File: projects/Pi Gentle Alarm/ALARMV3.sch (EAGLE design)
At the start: 6 parts, among them IC1 7805T, X1 RASPI_BOARD_B+_E0

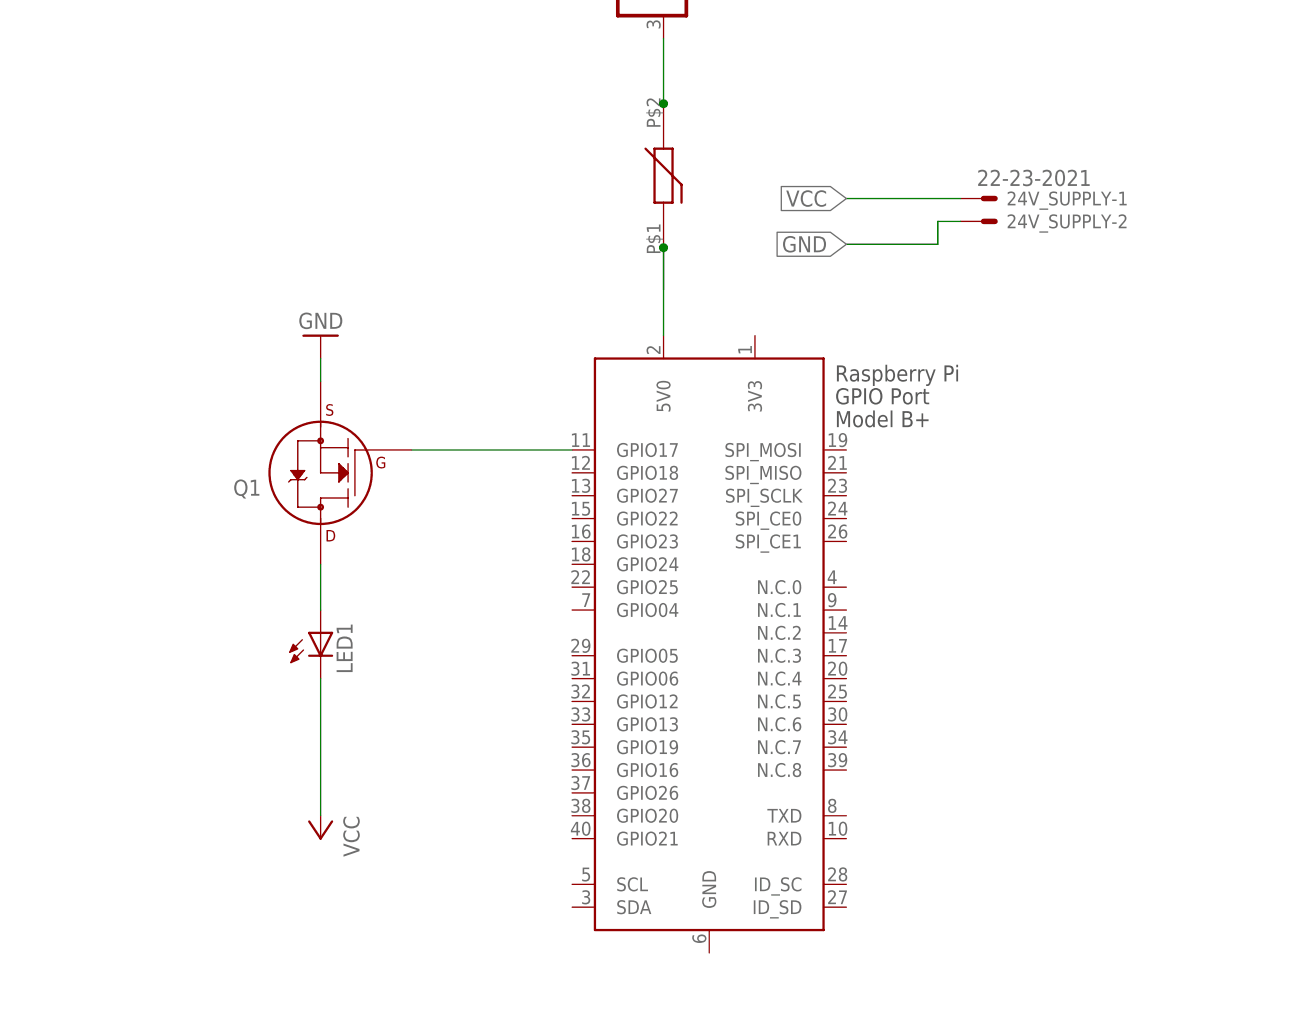
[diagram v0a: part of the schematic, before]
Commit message: Added a button for turning off the alarm
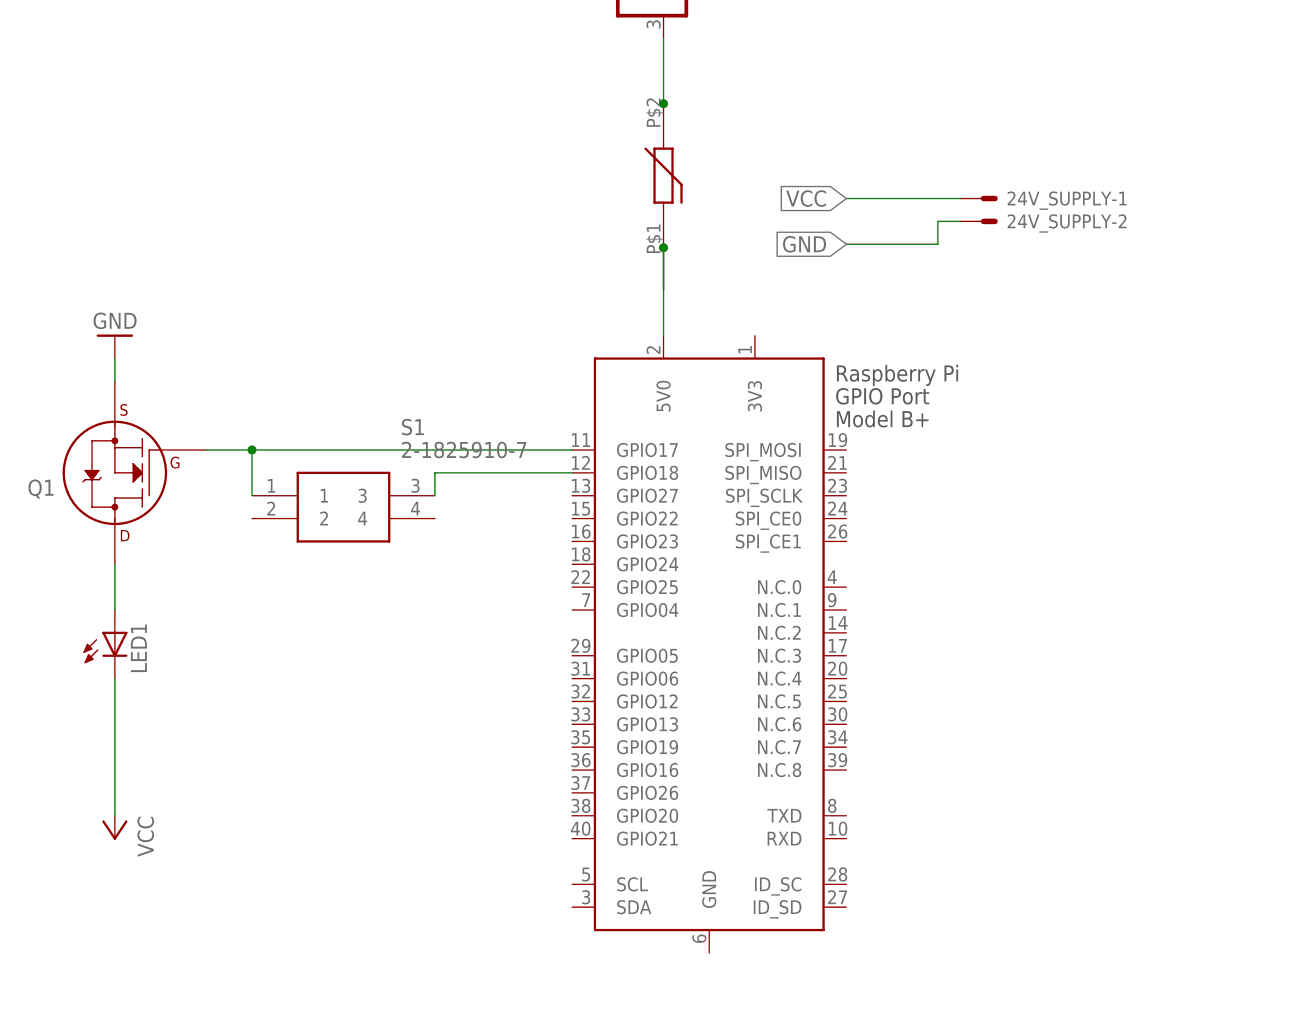
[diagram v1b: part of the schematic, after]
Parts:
- added S1: 2-1825910-7, SamacSys_Parts:2-1825910-7
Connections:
- new net N$3: S1.3, X1.GPIO18
- net GPIO17: now also S1.1
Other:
- moved on the sheet: LED1, Q1
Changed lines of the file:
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@@
 <part name="GND2" library="supply1" library_urn="urn:adsk.eagle:library:371" deviceset="GND" device=""/>
 <part name="F1" library="Test" deviceset="MF-MSMF260-2" device=""/>
+<part name="S1" library="SamacSys_Parts" deviceset="2-1825910-7" device=""/>
 </parts>
 <sheets>
@@
 <instance part="24V_SUPPLY" gate="-1" x="119.38" y="198.12" smashed="yes">
 <attribute name="NAME" x="121.92" y="197.358" size="1.524" layer="95"/>
-<attribute name="VALUE" x="118.618" y="199.517" size="1.778" layer="96"/>
 </instance>
 <instance part="24V_SUPPLY" gate="-2" x="119.38" y="195.58" smashed="yes">
 <attribute name="NAME" x="121.92" y="194.818" size="1.524" layer="95"/>
 </instance>
-<instance part="Q1" gate="G$1" x="45.72" y="167.64" smashed="yes" rot="R180">
-<attribute name="NAME" x="39.116" y="166.878" size="1.778" layer="95" rot="R180"/>
-<attribute name="VALUE" x="39.116" y="169.164" size="1.778" layer="96" rot="R180"/>
-<attribute name="OC_NEWARK" x="45.72" y="167.64" size="1.778" layer="96" display="off"/>
-<attribute name="MF" x="45.72" y="167.64" size="1.778" layer="96" display="off"/>
-<attribute name="MPN" x="45.72" y="167.64" size="1.778" layer="96" display="off"/>
+<instance part="Q1" gate="G$1" x="22.86" y="167.64" smashed="yes" rot="R180">
+<attribute name="NAME" x="16.256" y="166.878" size="1.778" layer="95" rot="R180"/>
+<attribute name="VALUE" x="16.256" y="169.164" size="1.778" layer="96" rot="R180"/>
+<attribute name="OC_NEWARK" x="22.86" y="167.64" size="1.778" layer="96" display="off"/>
+<attribute name="MF" x="22.86" y="167.64" size="1.778" layer="96" display="off"/>
+<attribute name="MPN" x="22.86" y="167.64" size="1.778" layer="96" display="off"/>
 </instance>
-<instance part="P+1" gate="VCC" x="45.72" y="127" smashed="yes" rot="R180">
-<attribute name="VALUE" x="48.26" y="129.54" size="1.778" layer="96" rot="R270"/>
+<instance part="P+1" gate="VCC" x="22.86" y="127" smashed="yes" rot="R180">
+<attribute name="VALUE" x="25.4" y="129.54" size="1.778" layer="96" rot="R270"/>
 </instance>
-<instance part="GND1" gate="1" x="45.72" y="182.88" smashed="yes" rot="R180">
-<attribute name="VALUE" x="48.26" y="185.42" size="1.778" layer="96" rot="R180"/>
+<instance part="GND1" gate="1" x="22.86" y="182.88" smashed="yes" rot="R180">
+<attribute name="VALUE" x="25.4" y="185.42" size="1.778" layer="96" rot="R180"/>
 </instance>
-<instance part="LED1" gate="G$1" x="45.72" y="149.86" smashed="yes">
-<attribute name="NAME" x="49.276" y="145.288" size="1.778" layer="95" rot="R90"/>
-<attribute name="VALUE" x="51.435" y="145.288" size="1.778" layer="96" rot="R90"/>
-<attribute name="OC_NEWARK" x="45.72" y="149.86" size="1.778" layer="96" display="off"/>
-<attribute name="MF" x="45.72" y="149.86" size="1.778" layer="96" display="off"/>
-<attribute name="MPN" x="45.72" y="149.86" size="1.778" layer="96" display="off"/>
+<instance part="LED1" gate="G$1" x="22.86" y="149.86" smashed="yes">
+<attribute name="NAME" x="26.416" y="145.288" size="1.778" layer="95" rot="R90"/>
+<attribute name="VALUE" x="28.575" y="145.288" size="1.778" layer="96" rot="R90"/>
+<attribute name="OC_NEWARK" x="22.86" y="149.86" size="1.778" layer="96" display="off"/>
+<attribute name="MF" x="22.86" y="149.86" size="1.778" layer="96" display="off"/>
+<attribute name="MPN" x="22.86" y="149.86" size="1.778" layer="96" display="off"/>
 </instance>
 <instance part="IC1" gate="A1" x="83.82" y="226.06" smashed="yes" rot="R270">
@@
 </instance>
 <instance part="F1" gate="G$1" x="83.82" y="200.66" smashed="yes" rot="R90"/>
+<instance part="S1" gate="G$1" x="38.1" y="165.1" smashed="yes">
+<attribute name="NAME" x="54.61" y="172.72" size="1.778" layer="95" align="center-left"/>
+<attribute name="VALUE" x="54.61" y="170.18" size="1.778" layer="96" align="center-left"/>
+</instance>
 </instances>
 <busses>
@@
 <segment>
 <pinref part="P+1" gate="VCC" pin="VCC"/>
-<wire x1="45.72" y1="144.78" x2="45.72" y2="129.54" width="0.1524" layer="91"/>
+<wire x1="22.86" y1="144.78" x2="22.86" y2="129.54" width="0.1524" layer="91"/>
 <pinref part="LED1" gate="G$1" pin="C"/>
 </segment>
@@
 <pinref part="Q1" gate="G$1" pin="S"/>
 <pinref part="GND1" gate="1" pin="GND"/>
-<wire x1="45.72" y1="177.8" x2="45.72" y2="180.34" width="0.1524" layer="91"/>
+<wire x1="22.86" y1="177.8" x2="22.86" y2="180.34" width="0.1524" layer="91"/>
 </segment>
 <segment>
@@
 <net name="GPIO17" class="0">
 <segment>
-<wire x1="73.66" y1="170.18" x2="55.88" y2="170.18" width="0.1524" layer="91"/>
+<wire x1="73.66" y1="170.18" x2="38.1" y2="170.18" width="0.1524" layer="91"/>
 <pinref part="Q1" gate="G$1" pin="G"/>
 <pinref part="X1" gate="G$1" pin="GPIO17"/>
+<pinref part="S1" gate="G$1" pin="1"/>
+<wire x1="38.1" y1="170.18" x2="33.02" y2="170.18" width="0.1524" layer="91"/>
+<wire x1="38.1" y1="165.1" x2="38.1" y2="170.18" width="0.1524" layer="91"/>
+<junction x="38.1" y="170.18"/>
 </segment>
 </net>
@@
 <segment>
 <pinref part="Q1" gate="G$1" pin="D"/>
-<wire x1="45.72" y1="152.4" x2="45.72" y2="157.48" width="0.1524" layer="91"/>
+<wire x1="22.86" y1="152.4" x2="22.86" y2="157.48" width="0.1524" layer="91"/>
 <pinref part="LED1" gate="G$1" pin="A"/>
 </segment>
@@
 </segment>
 </net>
+<net name="N$3" class="0">
+<segment>
+<pinref part="S1" gate="G$1" pin="3"/>
+<pinref part="X1" gate="G$1" pin="GPIO18"/>
+<wire x1="58.42" y1="165.1" x2="58.42" y2="167.64" width="0.1524" layer="91"/>
+<wire x1="58.42" y1="167.64" x2="73.66" y2="167.64" width="0.1524" layer="91"/>
+</segment>
+</net>

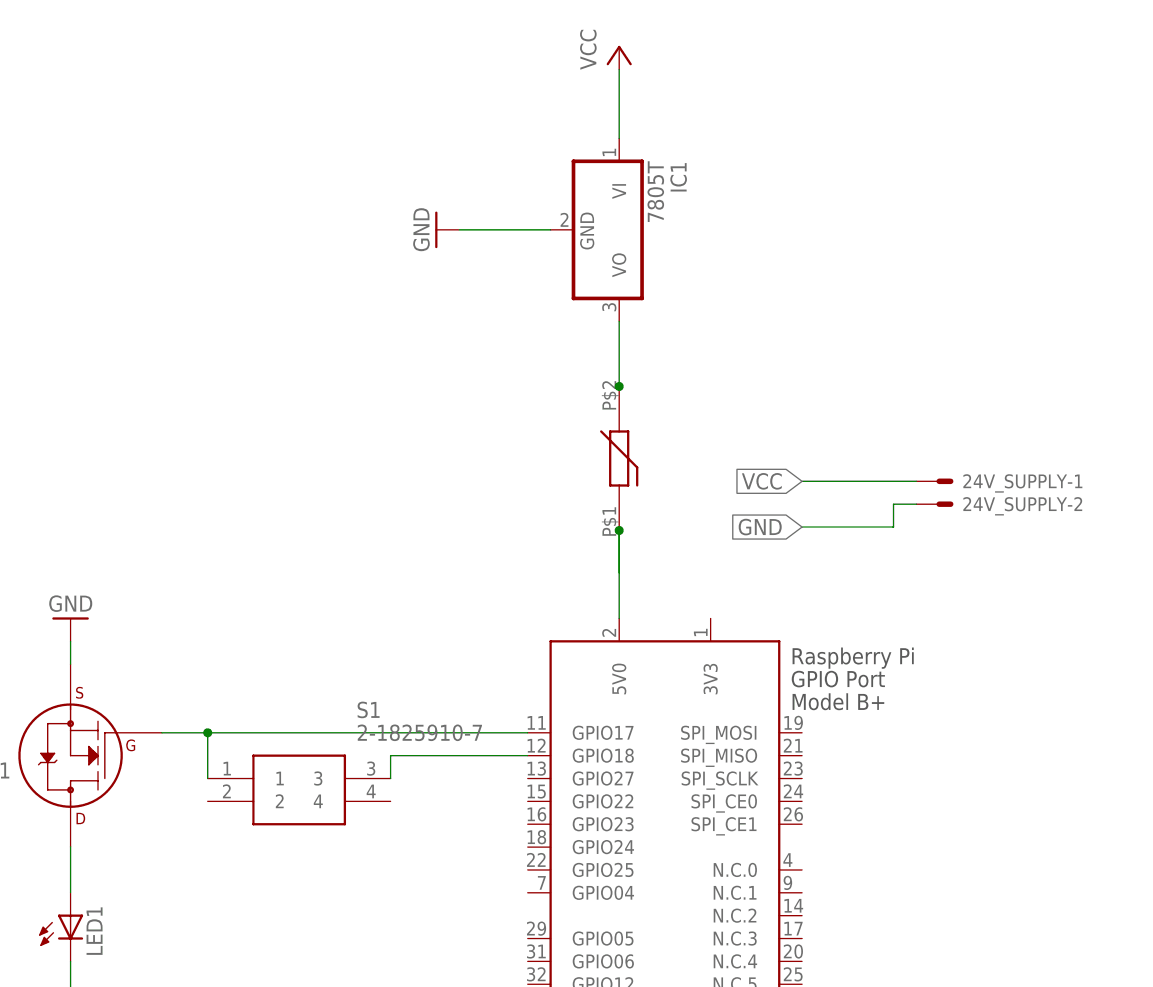
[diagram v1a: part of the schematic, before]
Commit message: Satisfied dependancies
Voltage regulator needed capacitors
Changed shut-off button
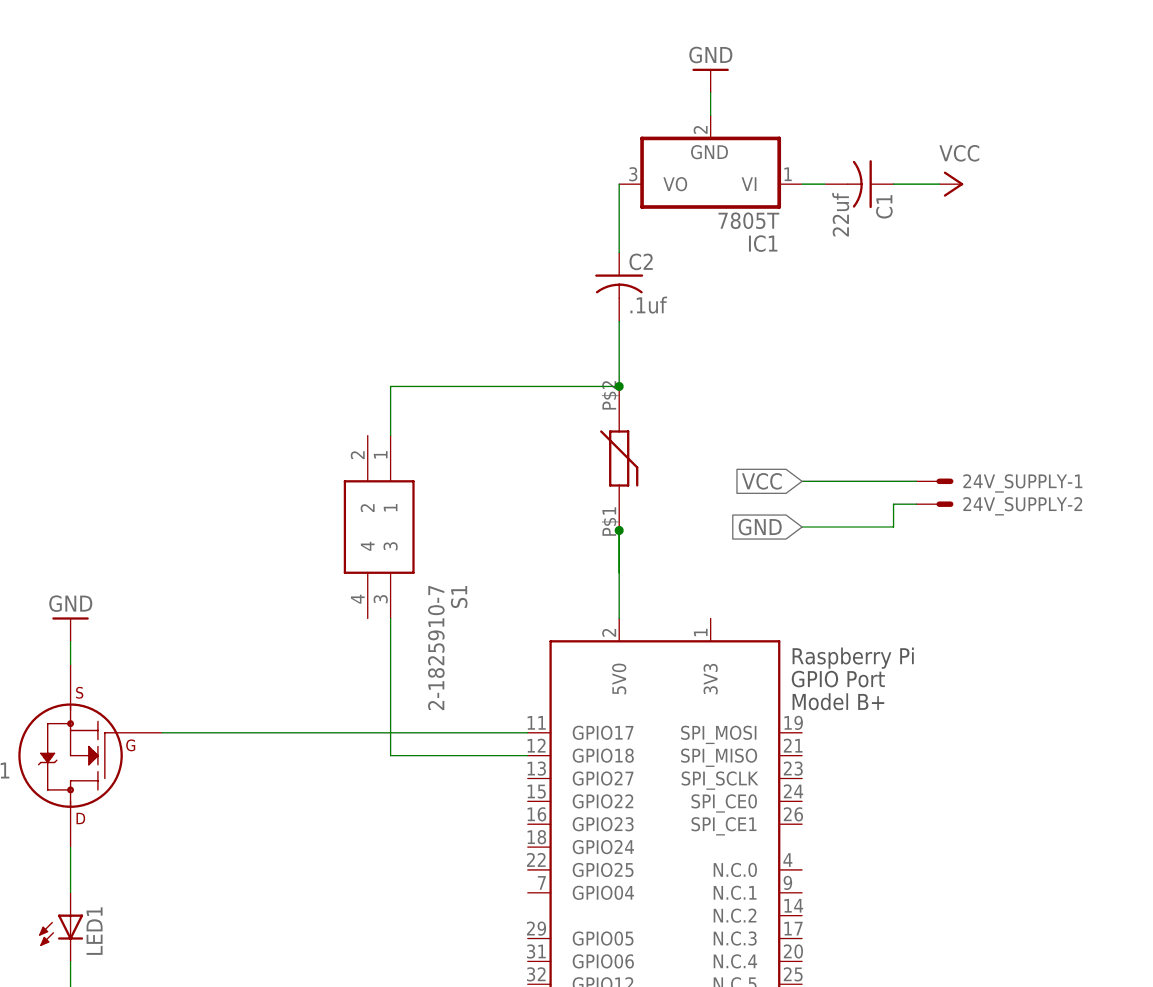
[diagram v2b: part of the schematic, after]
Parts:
- added C1: 22uf, adafruit:C-US050-024X044
- added C2: .1uf, adafruit:C-US050-024X044
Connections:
- new net N$4: C1.2, IC1.VI
- new net N$5: C2.1, IC1.VO
- net GPIO17: no longer S1.1
- net N$2: now also C2.2, S1.1; no longer IC1.VO
- net VCC: now also C1.1; no longer IC1.VI
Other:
- moved on the sheet: IC1, S1
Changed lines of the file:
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@@
 <part name="F1" library="Test" deviceset="MF-MSMF260-2" device=""/>
 <part name="S1" library="SamacSys_Parts" deviceset="2-1825910-7" device=""/>
+<part name="C1" library="adafruit" library_urn="urn:adsk.eagle:library:420" deviceset="C-US" device="050-024X044" package3d_urn="urn:adsk.eagle:package:6240356/1" value="22uf"/>
+<part name="C2" library="adafruit" library_urn="urn:adsk.eagle:library:420" deviceset="C-US" device="050-024X044" package3d_urn="urn:adsk.eagle:package:6240356/1" value=".1uf"/>
 </parts>
 <sheets>
@@
 <attribute name="MPN" x="22.86" y="149.86" size="1.778" layer="96" display="off"/>
 </instance>
-<instance part="IC1" gate="A1" x="83.82" y="226.06" smashed="yes" rot="R270">
-<attribute name="NAME" x="89.535" y="233.68" size="1.778" layer="95" rot="R270"/>
-<attribute name="VALUE" x="86.995" y="233.68" size="1.778" layer="96" rot="R270"/>
-<attribute name="OC_NEWARK" x="83.82" y="226.06" size="1.778" layer="96" display="off"/>
-<attribute name="MF" x="83.82" y="226.06" size="1.778" layer="96" display="off"/>
-<attribute name="MPN" x="83.82" y="226.06" size="1.778" layer="96" display="off"/>
+<instance part="IC1" gate="A1" x="93.98" y="231.14" smashed="yes" rot="R180">
+<attribute name="NAME" x="101.6" y="225.425" size="1.778" layer="95" rot="R180"/>
+<attribute name="VALUE" x="101.6" y="227.965" size="1.778" layer="96" rot="R180"/>
+<attribute name="OC_NEWARK" x="93.98" y="231.14" size="1.778" layer="96" rot="R270" display="off"/>
+<attribute name="MF" x="93.98" y="231.14" size="1.778" layer="96" rot="R270" display="off"/>
+<attribute name="MPN" x="93.98" y="231.14" size="1.778" layer="96" rot="R270" display="off"/>
 </instance>
-<instance part="P+2" gate="VCC" x="83.82" y="246.38" smashed="yes">
-<attribute name="VALUE" x="81.28" y="243.84" size="1.778" layer="96" rot="R90"/>
+<instance part="P+2" gate="VCC" x="121.92" y="231.14" smashed="yes" rot="R270">
+<attribute name="VALUE" x="119.38" y="233.68" size="1.778" layer="96"/>
 </instance>
-<instance part="GND2" gate="1" x="63.5" y="226.06" smashed="yes" rot="R270">
-<attribute name="VALUE" x="60.96" y="228.6" size="1.778" layer="96" rot="R270"/>
+<instance part="GND2" gate="1" x="93.98" y="243.84" smashed="yes" rot="R180">
+<attribute name="VALUE" x="96.52" y="246.38" size="1.778" layer="96" rot="R180"/>
 </instance>
 <instance part="F1" gate="G$1" x="83.82" y="200.66" smashed="yes" rot="R90"/>
-<instance part="S1" gate="G$1" x="38.1" y="165.1" smashed="yes">
-<attribute name="NAME" x="54.61" y="172.72" size="1.778" layer="95" align="center-left"/>
-<attribute name="VALUE" x="54.61" y="170.18" size="1.778" layer="96" align="center-left"/>
+<instance part="S1" gate="G$1" x="58.42" y="203.2" smashed="yes" rot="R270">
+<attribute name="NAME" x="66.04" y="186.69" size="1.778" layer="95" rot="R270" align="center-left"/>
+<attribute name="VALUE" x="63.5" y="186.69" size="1.778" layer="96" rot="R270" align="center-left"/>
+</instance>
+<instance part="C1" gate="G$1" x="111.76" y="231.14" smashed="yes" rot="R270">
+<attribute name="NAME" x="112.395" y="230.124" size="1.778" layer="95" rot="R270"/>
+<attribute name="VALUE" x="107.569" y="230.124" size="1.778" layer="96" rot="R270"/>
+</instance>
+<instance part="C2" gate="G$1" x="83.82" y="220.98" smashed="yes">
+<attribute name="NAME" x="84.836" y="221.615" size="1.778" layer="95"/>
+<attribute name="VALUE" x="84.836" y="216.789" size="1.778" layer="96"/>
 </instance>
 </instances>
@@
 </segment>
 <segment>
-<pinref part="IC1" gate="A1" pin="VI"/>
 <pinref part="P+2" gate="VCC" pin="VCC"/>
-<wire x1="83.82" y1="243.84" x2="83.82" y2="236.22" width="0.1524" layer="91"/>
+<pinref part="C1" gate="G$1" pin="1"/>
+<wire x1="119.38" y1="231.14" x2="114.3" y2="231.14" width="0.1524" layer="91"/>
 </segment>
 </net>
@@
 <pinref part="IC1" gate="A1" pin="GND"/>
 <pinref part="GND2" gate="1" pin="GND"/>
-<wire x1="66.04" y1="226.06" x2="76.2" y2="226.06" width="0.1524" layer="91"/>
+<wire x1="93.98" y1="241.3" x2="93.98" y2="238.76" width="0.1524" layer="91"/>
 </segment>
 </net>
 <net name="GPIO17" class="0">
 <segment>
-<wire x1="73.66" y1="170.18" x2="38.1" y2="170.18" width="0.1524" layer="91"/>
+<wire x1="73.66" y1="170.18" x2="33.02" y2="170.18" width="0.1524" layer="91"/>
 <pinref part="Q1" gate="G$1" pin="G"/>
 <pinref part="X1" gate="G$1" pin="GPIO17"/>
-<pinref part="S1" gate="G$1" pin="1"/>
-<wire x1="38.1" y1="170.18" x2="33.02" y2="170.18" width="0.1524" layer="91"/>
-<wire x1="38.1" y1="165.1" x2="38.1" y2="170.18" width="0.1524" layer="91"/>
-<junction x="38.1" y="170.18"/>
 </segment>
 </net>
@@
 <net name="N$2" class="0">
 <segment>
-<pinref part="IC1" gate="A1" pin="VO"/>
 <wire x1="83.82" y1="208.28" x2="83.82" y2="208.66" width="0.1524" layer="91"/>
 <pinref part="F1" gate="G$1" pin="P$2"/>
-<wire x1="83.82" y1="208.66" x2="83.82" y2="215.9" width="0.1524" layer="91"/>
 <junction x="83.82" y="208.66"/>
+<pinref part="S1" gate="G$1" pin="1"/>
+<wire x1="83.82" y1="208.66" x2="58.42" y2="208.66" width="0.1524" layer="91"/>
+<wire x1="58.42" y1="208.66" x2="58.42" y2="203.2" width="0.1524" layer="91"/>
+<pinref part="C2" gate="G$1" pin="2"/>
+<wire x1="83.82" y1="215.9" x2="83.82" y2="208.66" width="0.1524" layer="91"/>
 </segment>
 </net>
@@
 <pinref part="S1" gate="G$1" pin="3"/>
 <pinref part="X1" gate="G$1" pin="GPIO18"/>
-<wire x1="58.42" y1="165.1" x2="58.42" y2="167.64" width="0.1524" layer="91"/>
+<wire x1="58.42" y1="182.88" x2="58.42" y2="167.64" width="0.1524" layer="91"/>
 <wire x1="58.42" y1="167.64" x2="73.66" y2="167.64" width="0.1524" layer="91"/>
 </segment>
 </net>
+<net name="N$4" class="0">
+<segment>
+<pinref part="IC1" gate="A1" pin="VI"/>
+<pinref part="C1" gate="G$1" pin="2"/>
+<wire x1="106.68" y1="231.14" x2="104.14" y2="231.14" width="0.1524" layer="91"/>
+</segment>
+</net>
+<net name="N$5" class="0">
+<segment>
+<pinref part="IC1" gate="A1" pin="VO"/>
+<pinref part="C2" gate="G$1" pin="1"/>
+<wire x1="83.82" y1="231.14" x2="83.82" y2="223.52" width="0.1524" layer="91"/>
+</segment>
+</net>
